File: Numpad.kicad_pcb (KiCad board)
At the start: 2 copper layers, 106 parts, among them J1 USB_C_Receptacle_USB2.0, J3 AVR-ISP-6, Q101 DMN2041L, Q2 DMN2041L, SW10 SW_Push, SW11 SW_Push, SW12 SW_Push, SW13 SW_Push, SW14 SW_Push, SW15 SW_Push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

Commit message: some changes iuno
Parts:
- moved C7 127.0 mm to (51.8, 19.3)
- moved C3 118.6 mm to (70.6, 12.2), turned to 180 degrees
- moved R121 116.6 mm to (68.2, 8.51), turned to 180 degrees
- moved C5 115.3 mm to (70.6, 16.8), turned to 180 degrees
- moved Y1 114.8 mm to (70.6, 14.5), turned to 0 degrees
- moved R23 113.7 mm to (68.2, 9.53), turned to 180 degrees
- moved R6 113.5 mm to (57.4, 23.8)
- moved U1 113.2 mm to (60.3, 14.7)
- moved C4 113.1 mm to (60.7, 6.32), turned to 0 degrees
- moved C1 113.0 mm to (64.1, 23.3)
- moved R44 112.9 mm to (58.1, 5.84)
- moved R2 112.8 mm to (59.2, 5.87)
- moved C6 112.5 mm to (56.6, 6.32)
- moved R34 112.4 mm to (56.3, 23.8), turned to -90 degrees
- moved C2 101.9 mm to (68.6, 11.0), turned to -90 degrees
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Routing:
- net +5V: track 0.00 -> 12.1 mm
- net RST: track 0.00 -> 3.21 mm
- net NUM_LOCK_PWM: track 0.00 -> 3.09 mm
- net PWM: track 0.00 -> 2.91 mm
- net Net-(R34-Pad1): track 0.00 -> 2.90 mm
- net Net-(C4-Pad1): track 0.00 -> 2.74 mm

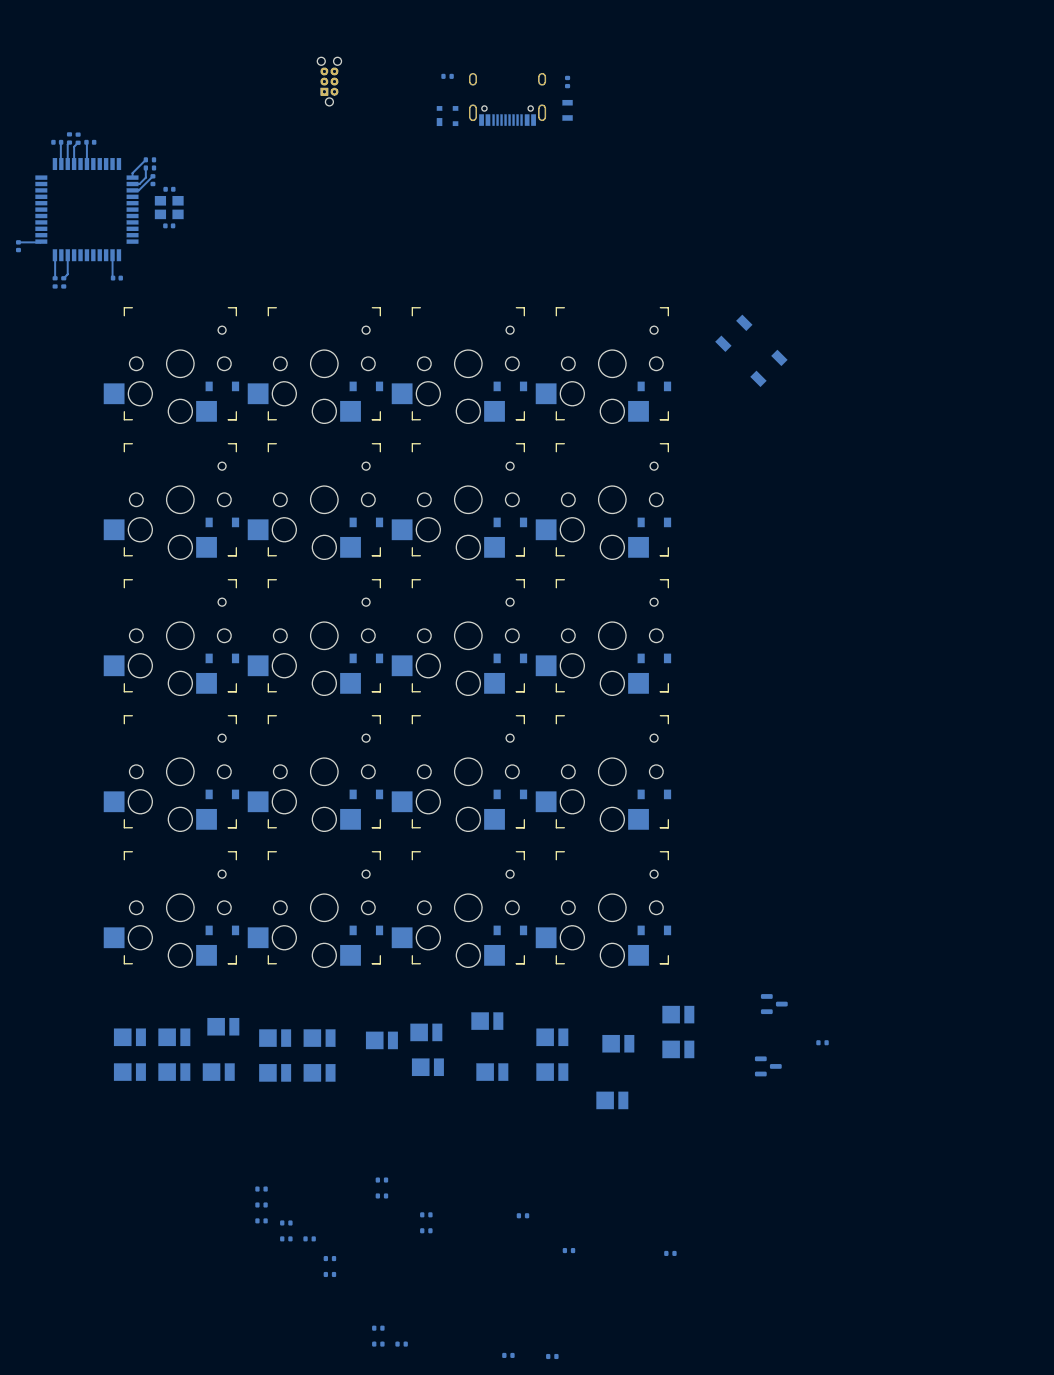
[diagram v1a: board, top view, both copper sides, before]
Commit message: switched atmega32u4 to u2 for the smaller footprint
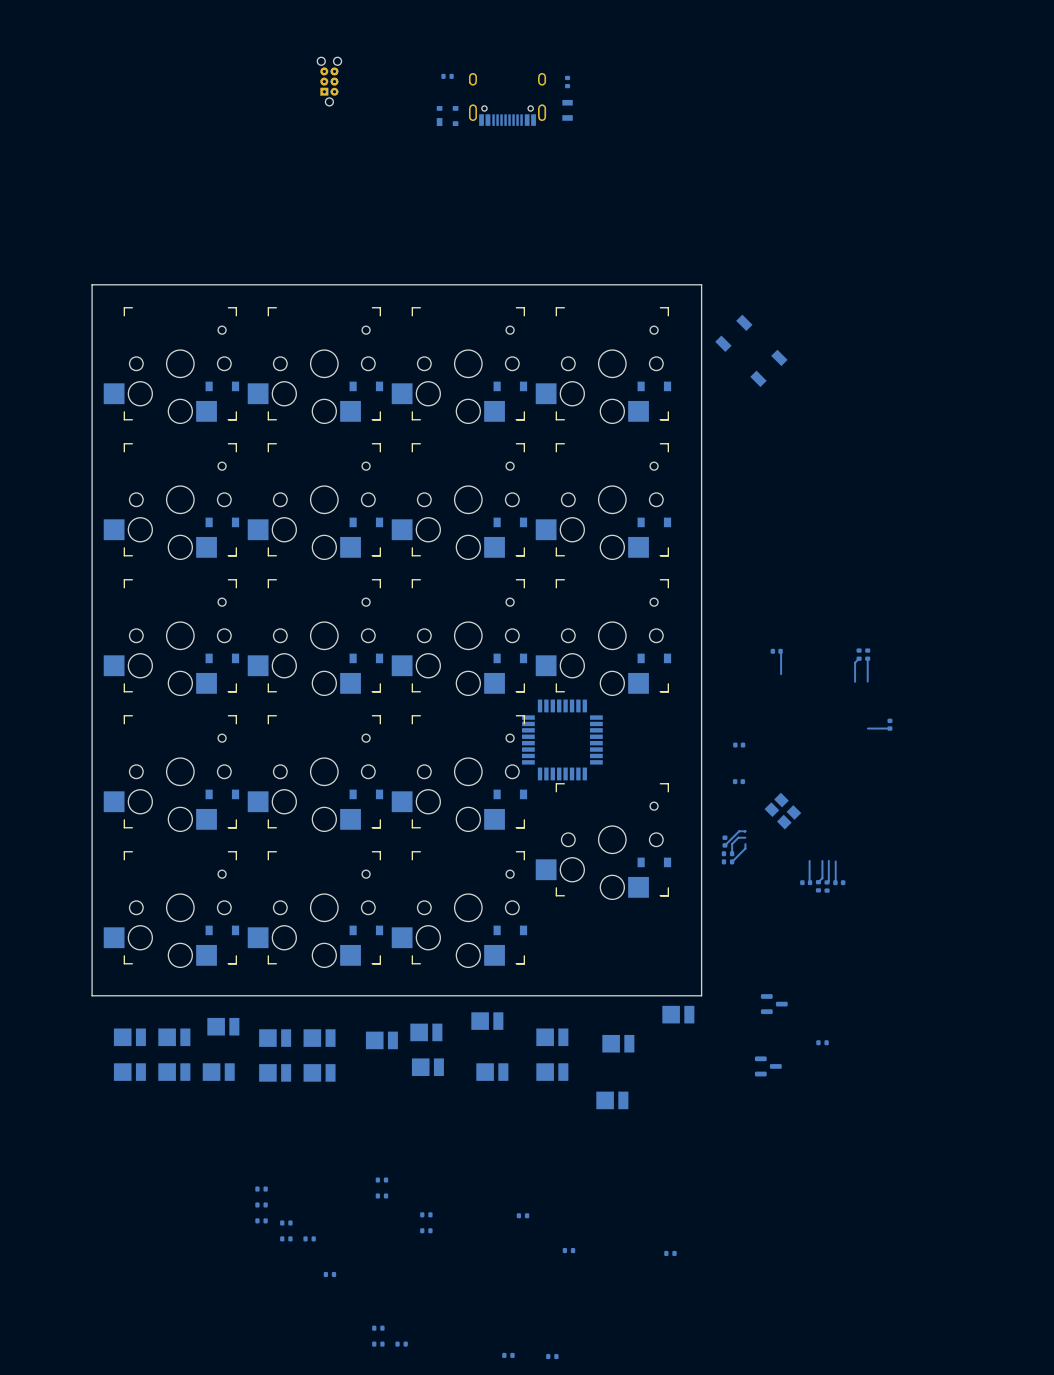
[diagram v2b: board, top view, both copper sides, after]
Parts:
- removed D116: LED, LED_SMD:LED_PLCC_2835
- removed D20: D_Small, Diode_SMD:D_SOD-123
- removed R116: 470, Resistor_SMD:R_0402_1005Metric
- removed SW20: SW_Push, keyswitches.pretty-2:Kailh_socket_PG1350
- U1: value ATmega32U4-A -> ATmega32U2-A; footprint Package_QFP:TQFP-44_10x10mm_P0.8mm -> Package_QFP:TQFP-32_7x7mm_P0.8mm
- moved C6 134.6 mm to (154.4, 98.9), turned to 0 degrees
- moved R44 133.1 mm to (152.8, 99.3), turned to 90 degrees
- moved R2 131.5 mm to (151.8, 99.3), turned to 90 degrees
- moved C4 128.7 mm to (150.2, 98.9), turned to 180 degrees
- moved C7 124.3 mm to (160.7, 79.1), turned to 90 degrees
- moved R121 113.7 mm to (140.5, 96.3), turned to 0 degrees
- moved R23 112.1 mm to (140.5, 95.2), turned to 0 degrees
- moved R34 111.7 mm to (157.9, 70.4), turned to 90 degrees
- moved R6 109.8 mm to (156.8, 70.4), turned to -90 degrees
- moved C2 109.3 mm to (140.1, 93.7), turned to 90 degrees
- moved Y1 107.6 mm to (147.3, 89.9), turned to 135 degrees
- moved C3 102.7 mm to (141.8, 86.2), turned to 0 degrees
- moved C5 96.4 mm to (141.9, 81.7), turned to 0 degrees
- moved C1 94.8 mm to (146.5, 69.9), turned to 180 degrees
- moved U1 89.0 mm to (119.8, 81.0), turned to 0 degrees
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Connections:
- U1 pad 1: unconnected-(U1-Pad1) -> Net-(C3-Pad2)
- U1 pad 10: MOSI -> ROW_1
- U1 pad 11: MISO -> ROW_0
- U1 pad 12: PWM -> ROW_2
- U1 pad 13: RST -> Net-(R34-Pad1)
- U1 pad 14: +5V -> ROW_3
- U1 pad 15: GND -> ROW_4
- U1 pad 16: Net-(C5-Pad1) -> unconnected-(U1-Pad16)
- U1 pad 17: Net-(C3-Pad2) -> COL_0
- U1 pad 18: unconnected-(U1-Pad18) -> COL_1
- U1 pad 19: unconnected-(U1-Pad19) -> COL_2
- U1 pad 2: +5V -> Net-(C5-Pad1)
- U1 pad 20: unconnected-(U1-Pad20) -> COL_3
- U1 pad 21: unconnected-(U1-Pad21) -> NUM_LOCK_PWM
- U1 pad 22: ROW_0 -> unconnected-(U1-Pad22)
- U1 pad 23: GND -> PWM
- U1 pad 24: +5V -> RST
- U1 pad 25: ROW_1 -> unconnected-(U1-Pad25)
- U1 pad 26: ROW_2 -> unconnected-(U1-Pad26)
- U1 pad 27: ROW_3 -> Net-(C4-Pad1)
- U1 pad 28: ROW_4 -> GND
- U1 pad 29: unconnected-(U1-Pad29) -> Net-(R2-Pad2)
- U1 pad 3: Net-(R44-Pad2) -> GND
- U1 pad 30: unconnected-(U1-Pad30) -> Net-(R44-Pad2)
- U1 pad 31: NUM_LOCK_PWM -> +5V
- U1 pad 32: unconnected-(U1-Pad32) -> +5V
- U1 pad 4: Net-(R2-Pad2) -> +5V
- U1 pad 5: GND -> unconnected-(U1-Pad5)
- U1 pad 6: Net-(C4-Pad1) -> SCLK
- U1 pad 7: +5V -> MOSI
- U1 pad 8: unconnected-(U1-Pad8) -> MISO
- U1 pad 9: SCLK -> unconnected-(U1-Pad9)
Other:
- board outline added: 76.2 x 88.9 mm

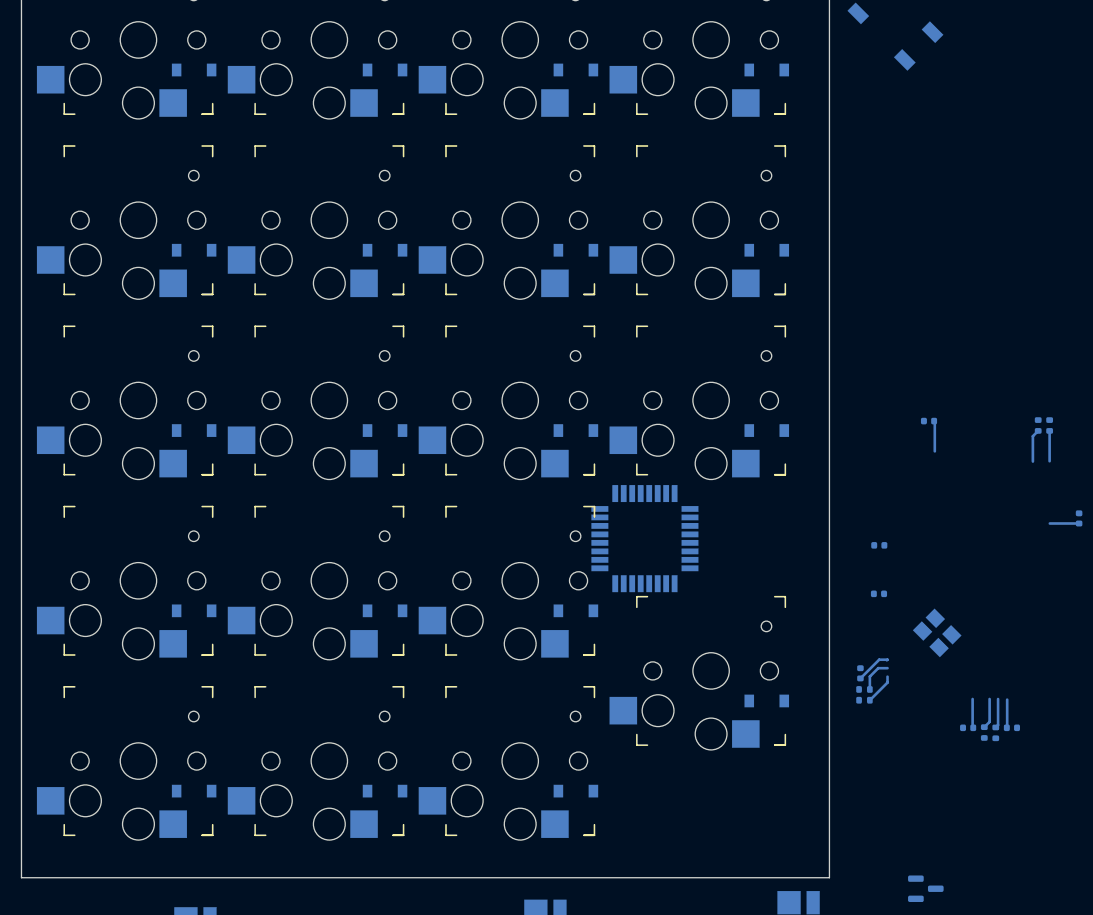
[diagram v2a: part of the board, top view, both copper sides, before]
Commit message: added some routing
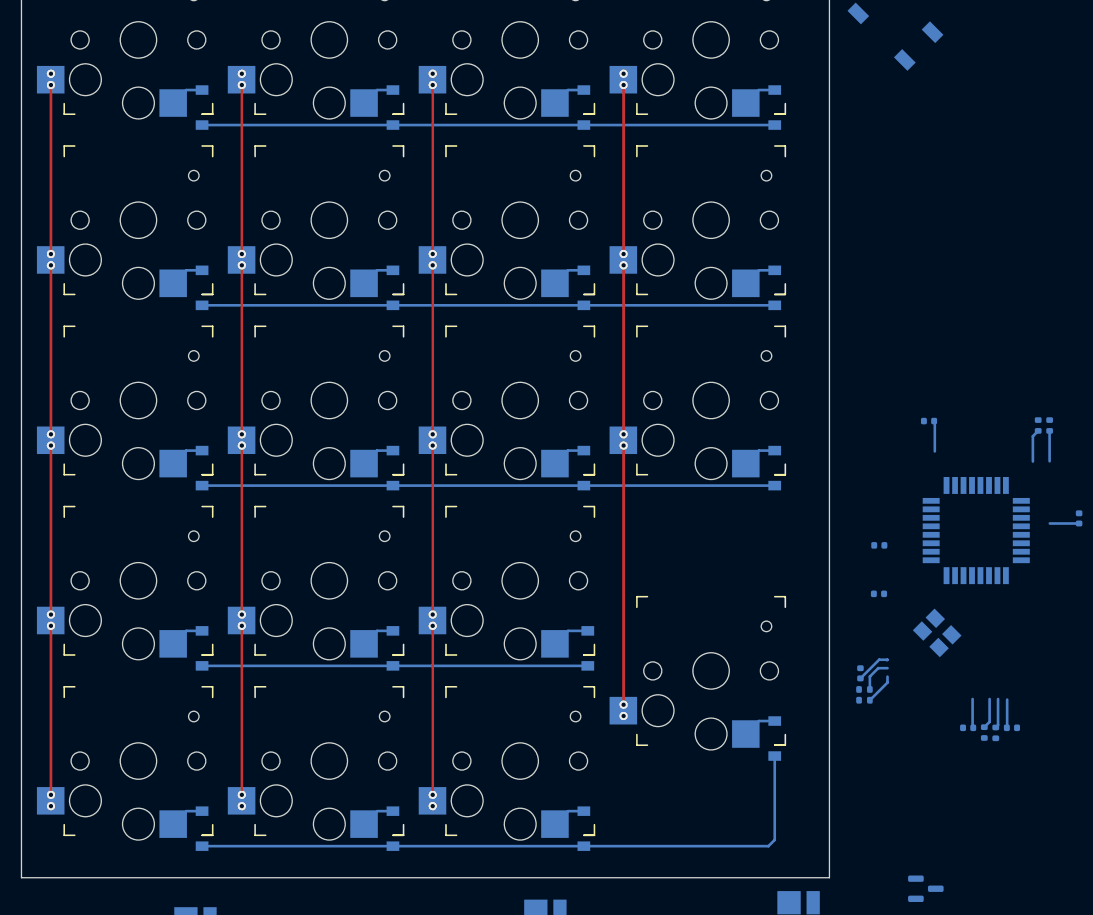
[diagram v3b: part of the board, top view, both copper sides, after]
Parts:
- moved U1 31.3 mm to (151.0, 80.3)
- moved D15 3.72 mm to (114.4, 91.4), turned to 90 degrees
- moved D16 3.62 mm to (114.0, 108.4), turned to 90 degrees
- moved D6 3.62 mm to (78.0, 108.4), turned to 90 degrees
- moved D19 3.62 mm to (132.0, 74.4), turned to 90 degrees
- moved D9 3.62 mm to (96.0, 74.4), turned to 90 degrees
- moved D11 3.62 mm to (96.0, 108.4), turned to 90 degrees
- moved D10 3.62 mm to (96.0, 91.4), turned to 90 degrees
- moved D21 3.62 mm to (132.0, 99.9), turned to 90 degrees
- moved D5 3.62 mm to (78.0, 91.4), turned to 90 degrees
- moved D14 3.62 mm to (114.0, 74.4), turned to 90 degrees
- moved D4 3.62 mm to (78.0, 74.4), turned to 90 degrees
- moved D13 3.62 mm to (114.0, 57.4), turned to 90 degrees
- moved D18 3.62 mm to (132.0, 57.4), turned to 90 degrees
- moved D3 3.62 mm to (78.0, 57.4), turned to 90 degrees
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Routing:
- net COL_2: track 0.00 -> 63.8 mm, vias 0 -> 10
- net COL_1: track 0.00 -> 63.8 mm, vias 0 -> 10
- net COL_0: track 0.00 -> 63.8 mm, vias 0 -> 10
- net ROW_0: track 0.00 -> 62.2 mm
- net COL_3: track 0.00 -> 56.3 mm, vias 0 -> 8
- net ROW_4: track 0.00 -> 54.0 mm
- net ROW_3: track 0.00 -> 54.0 mm
- net ROW_2: track 0.00 -> 54.0 mm
- net ROW_1: track 0.00 -> 36.4 mm
- net Net-(D15-Pad2): track 0.00 -> 3.61 mm
- net Net-(D7-Pad2): track 0.00 -> 3.23 mm
- net Net-(D2-Pad2): track 0.00 -> 3.23 mm
- net Net-(D12-Pad2): track 0.00 -> 3.23 mm
- net Net-(D17-Pad2): track 0.00 -> 3.23 mm
- net Net-(D8-Pad2): track 0.00 -> 3.23 mm
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
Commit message: more routing
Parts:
- moved R44 107.1 mm to (110.9, 0.76), turned to -90 degrees
- moved R2 105.1 mm to (115.2, 0.76), turned to -90 degrees
- moved D1 7.83 mm to (113.0, 1.27)
- moved J1 7.11 mm to (113.0, -7.62)
- moved R31 5.20 mm to (109.9, 0.76), turned to -90 degrees
- moved R22 4.64 mm to (116.2, 0.76), turned to -90 degrees
- moved F1 2.92 mm to (117.7, 1.14), turned to -90 degrees
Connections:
- D1 pad 2: D+ -> D-
- D1 pad 3: D- -> D+
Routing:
- net VCC: track 0.00 -> 12.4 mm, vias 0 -> 2
- net D-: track 0.00 -> 8.79 mm
- net D+: track 0.00 -> 7.32 mm
- net Net-(J1-PadA5): track 0.00 -> 4.62 mm
- net Net-(J1-PadB5): track 0.00 -> 4.42 mm
